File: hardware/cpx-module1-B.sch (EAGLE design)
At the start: 41 parts, among them IC2 MCP6004, IC3 LM4040DIM3-5.0, J1 WQP-PJ301M-12_JACK, J2 WQP-PJ301M-12_JACK, J3 WQP-PJ301M-12_JACK, J4 WQP-PJ301M-12_JACK, J5 WQP-PJ301M-12_JACK, J6 WQP-PJ301M-12_JACK, J7 WQP-PJ301M-12_JACK, J8 WQP-PJ301M-12_JACK, U1 CIRCUITPLAYGROUNDEXPRESS

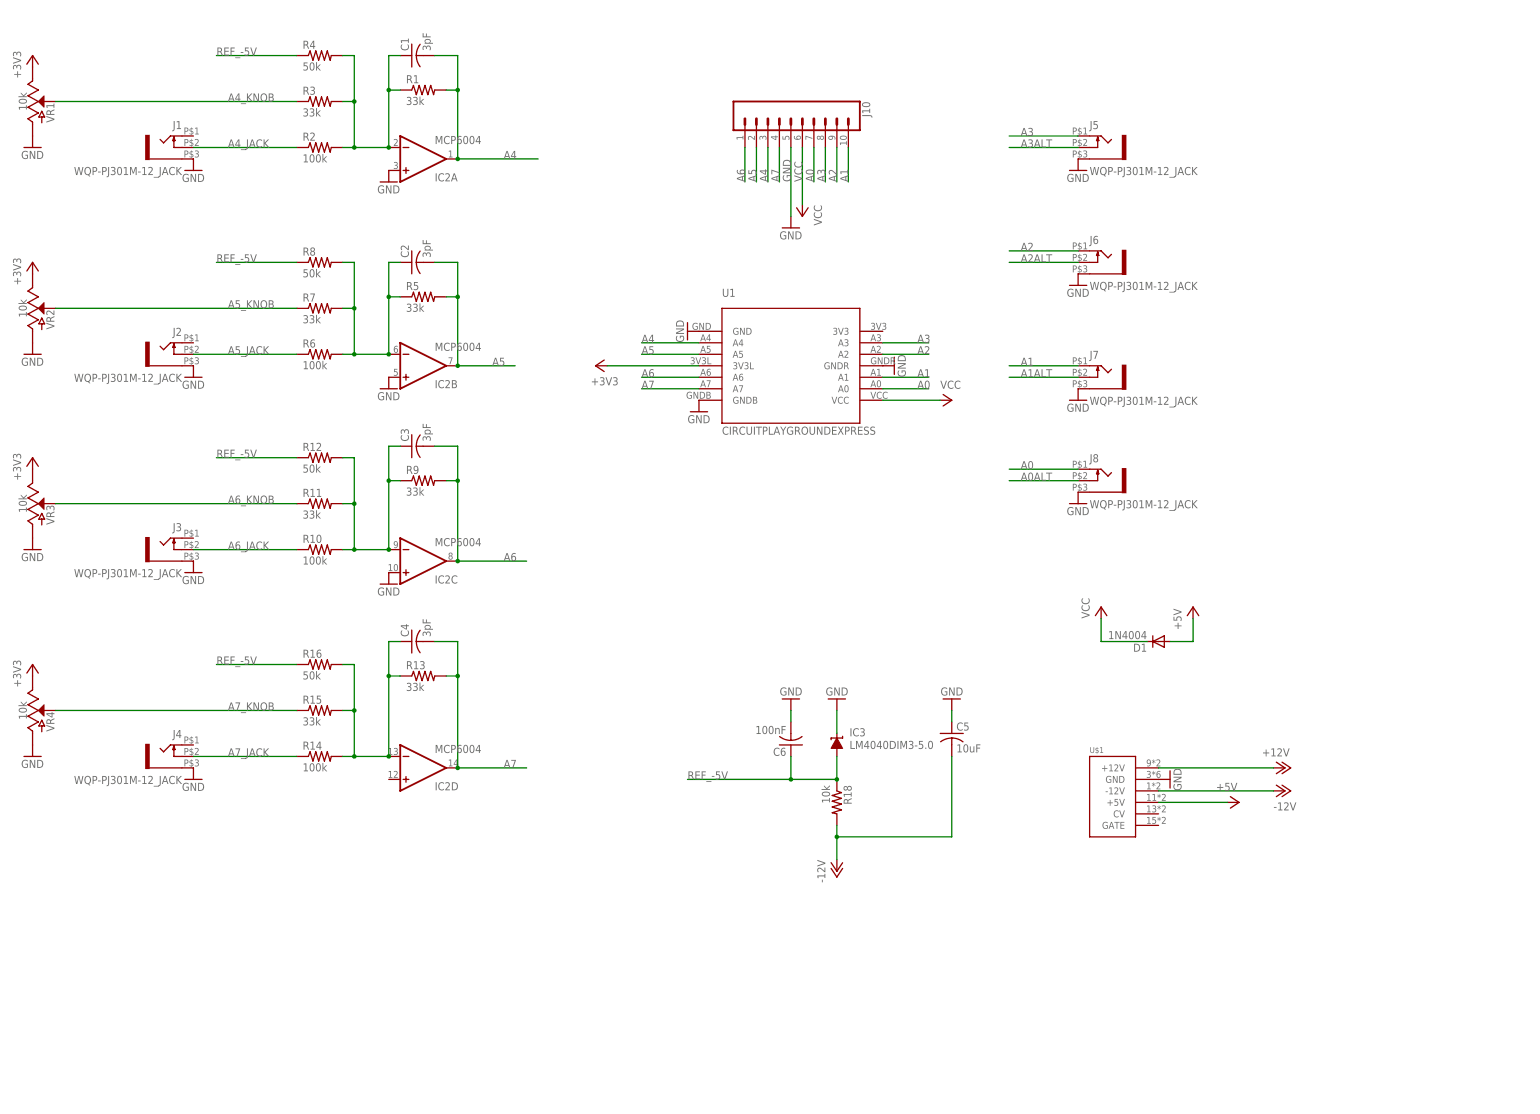
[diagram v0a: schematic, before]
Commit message: first cut at component placement
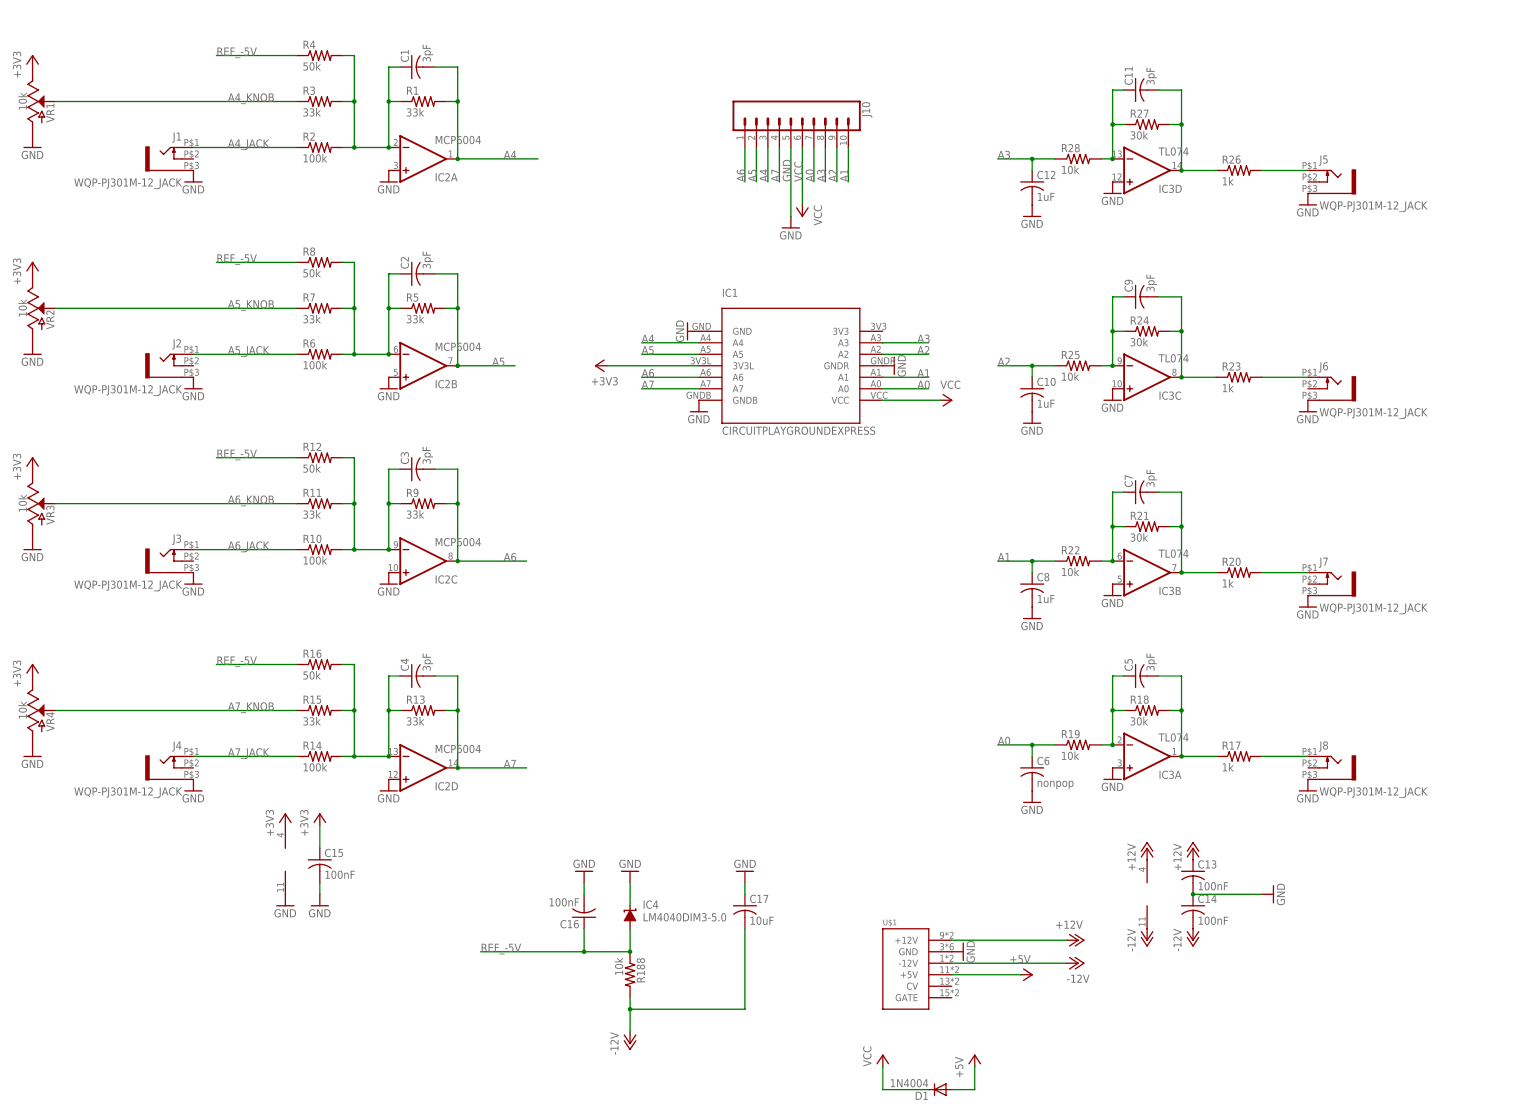
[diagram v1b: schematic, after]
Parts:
- added C10, C12, C8: 1uF, rcl:C-USC0603
- added C11, C7, C9: 3pF, rcl:C-USC0603
- added C13, C14, C15, C16: 100nF, rcl:C-USC0603
- added C17: 10uF, rcl:C-USC0603
- added IC4: LM4040DIM3-5.0, texas:LM4041B12DBZ
- added R17, R20, R23, R26: 1k, adafruit:R-US_R0603
- added R188, R19, R22, R25, R28: 10k, adafruit:R-US_R0603
- added R21, R24, R27: 30k, adafruit:R-US_R0603
- C5: value 10uF -> 3pF
- C6: value 100nF -> nonpop
- IC3: value LM4040DIM3-5.0 -> TL074; device texas:LM4041B12DBZ -> gm-ics:TL074D
- R18: value 10k -> 30k
- renumbered U1 to IC1
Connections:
- removed net A0ALT: J8.3
- removed net A1ALT: J7.3
- removed net A2ALT: J6.3
- removed net A3ALT: J5.3
- new net N$1: C5.2, IC3A.OUT, R17.1, R18.2
- new net N$10: C9.2, IC3C.OUT, R23.1, R24.2
- new net N$11: J7.2, R20.2
- new net N$12: C9.1, IC3C.-IN, R24.1, R25.2
- new net N$13: J6.2, R23.2
- new net N$14: C11.2, IC3D.OUT, R26.1, R27.2
- new net N$15: C11.1, IC3D.-IN, R27.1, R28.2
- new net N$16: J5.2, R26.2
- new net N$6: J8.2, R17.2
- new net N$7: C5.1, IC3A.-IN, R18.1, R19.2
- new net N$8: C7.2, IC3B.OUT, R20.1, R21.2
- new net N$9: C7.1, IC3B.-IN, R21.1, R22.2
- net +12V: now also C13.1, IC3P.V+
- net +3V3: now also C15.1, IC2P.V+
- net -12V: now also C14.2, C17.2, IC3P.V-, R188.2; no longer C5.2, R18.2
- net A0: now also C6.1, R19.1; no longer J8.2
- net A1: now also C8.1, R22.1; no longer J7.2
- net A2: now also C10.1, R25.1; no longer J6.2
- net A3: now also C12.1, R28.1; no longer J5.2
- net A4_JACK: now also J1.2; no longer J1.3
- net A5_JACK: now also J2.2; no longer J2.3
- net A6_JACK: now also J3.2; no longer J3.3
- net A7_JACK: now also J4.2; no longer J4.3
- net GND: now also C10.2, C12.2, C13.2, C14.1, C15.2, C16.2, C17.1, C8.2, IC2D.+IN, IC2P.V-, IC3A.+IN, IC3B.+IN, IC3C.+IN, IC3D.+IN, IC4.C; no longer C5.1, IC3.C
- net REF_-5V: now also C16.1, IC4.A, R188.1; no longer C6.1, IC3.A, R18.1
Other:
- moved on the sheet: C1, C2, C3, C4, C5, C6, D1, J1, J2, J3, J4, J5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

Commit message: autorouted as a test
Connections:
- net A4_KNOB: now also R3.1
- net A5_KNOB: now also R7.1
- net A6_KNOB: now also R11.1
- net A7_KNOB: now also R15.1
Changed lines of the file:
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@@
 <pinref part="VR1" gate="G$1" pin="S"/>
 <label x="-48.26" y="129.54" size="1.778" layer="95"/>
+<pinref part="R3" gate="G$1" pin="1"/>
 </segment>
 </net>
@@
 <pinref part="VR2" gate="G$1" pin="S"/>
 <label x="-48.26" y="83.82" size="1.778" layer="95"/>
+<pinref part="R7" gate="G$1" pin="1"/>
 </segment>
 </net>
@@
 <pinref part="VR3" gate="G$1" pin="S"/>
 <label x="-48.26" y="40.64" size="1.778" layer="95"/>
+<pinref part="R11" gate="G$1" pin="1"/>
 </segment>
 </net>
@@
 <pinref part="VR4" gate="G$1" pin="S"/>
 <label x="-48.26" y="-5.08" size="1.778" layer="95"/>
+<pinref part="R15" gate="G$1" pin="1"/>
 </segment>
 </net>

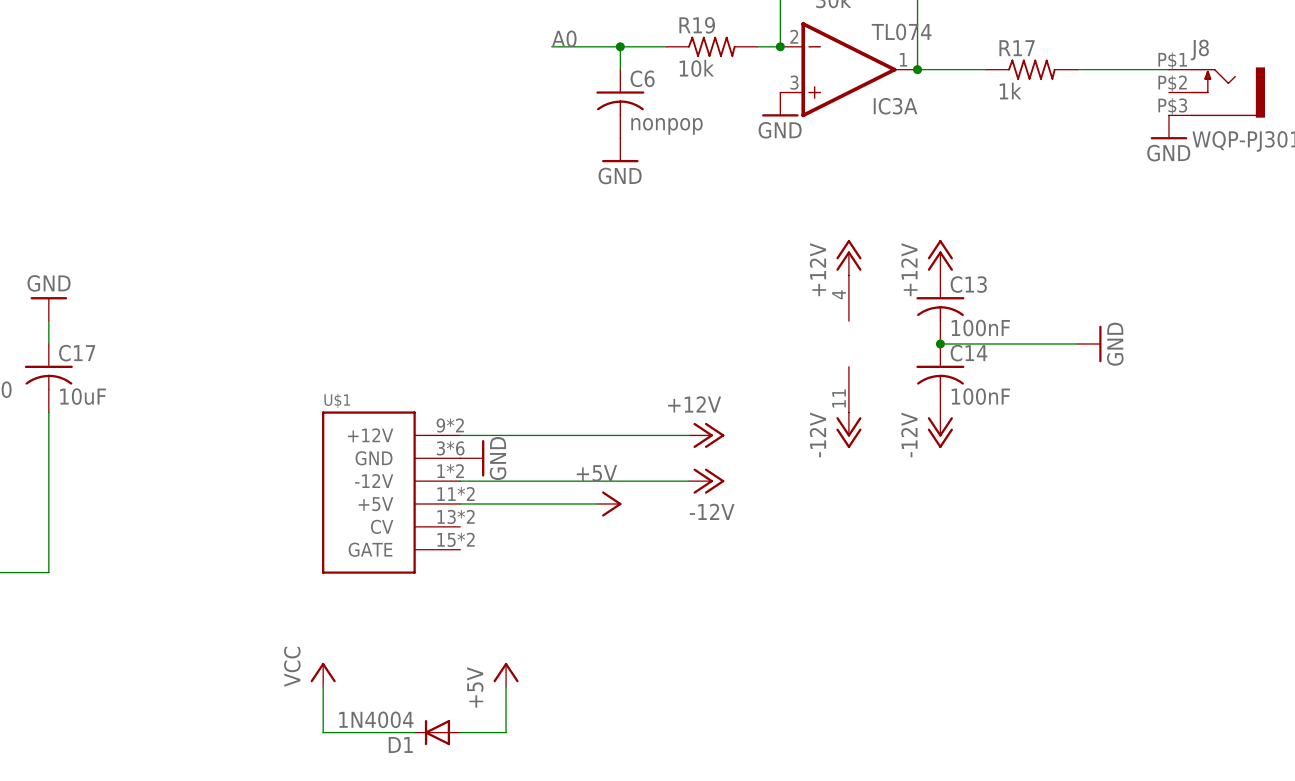
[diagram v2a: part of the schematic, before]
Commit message: added protection diodes and filter caps, added pdfs
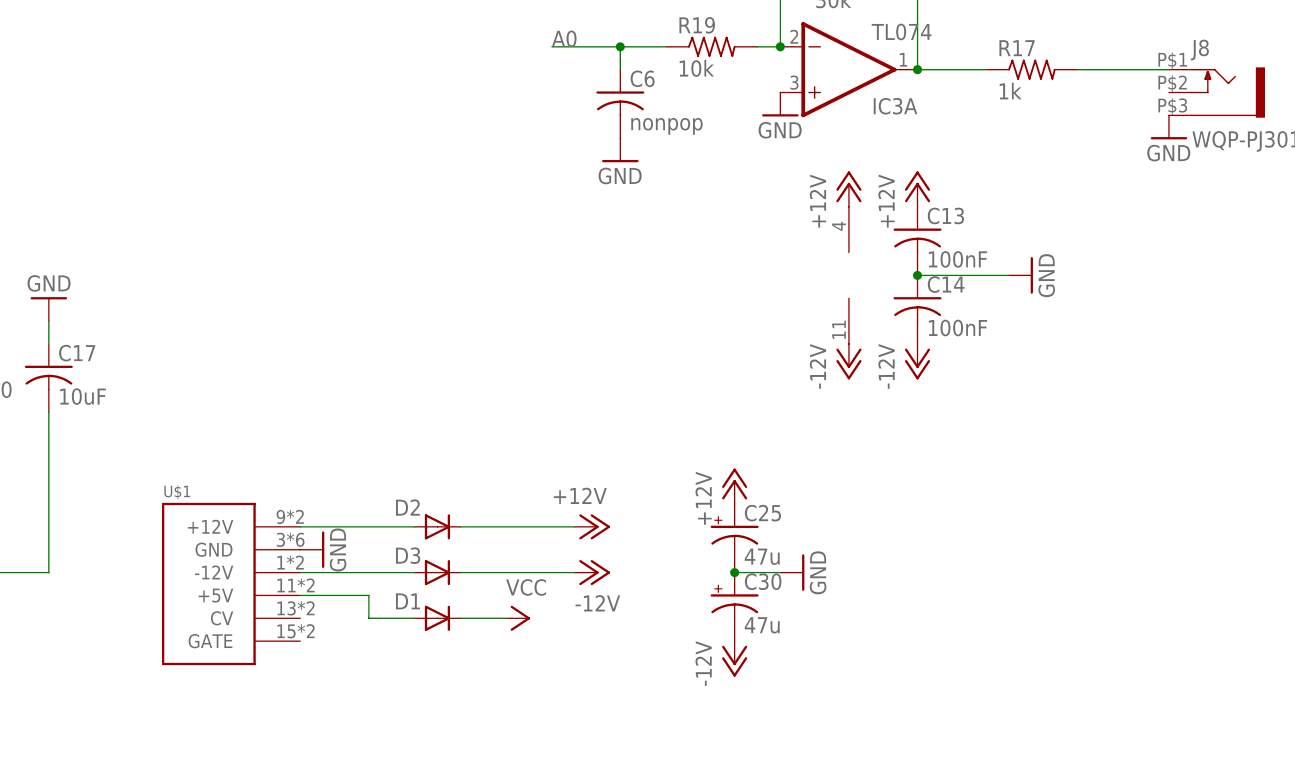
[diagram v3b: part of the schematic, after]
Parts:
- added C25, C30: 47u, rcl:CPOL-USD
- added D2, D3: 1N5819HW, diode:DIODE-SOD123
- D1: value 1N4004 -> 1N5819HW; device adafruit:1N4004 -> diode:DIODE-SOD123
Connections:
- net +5V renamed N$19
- new net N$17: D2.A, U$1.+12V
- new net N$18: D3.A, U$1.-12V
- net +12V: now also C25.+, D2.C; no longer U$1.+12V
- net -12V: now also C30.-, D3.C; no longer U$1.-12V
- net GND: now also C25.-, C30.+
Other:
- moved on the sheet: C13, C14, U$1

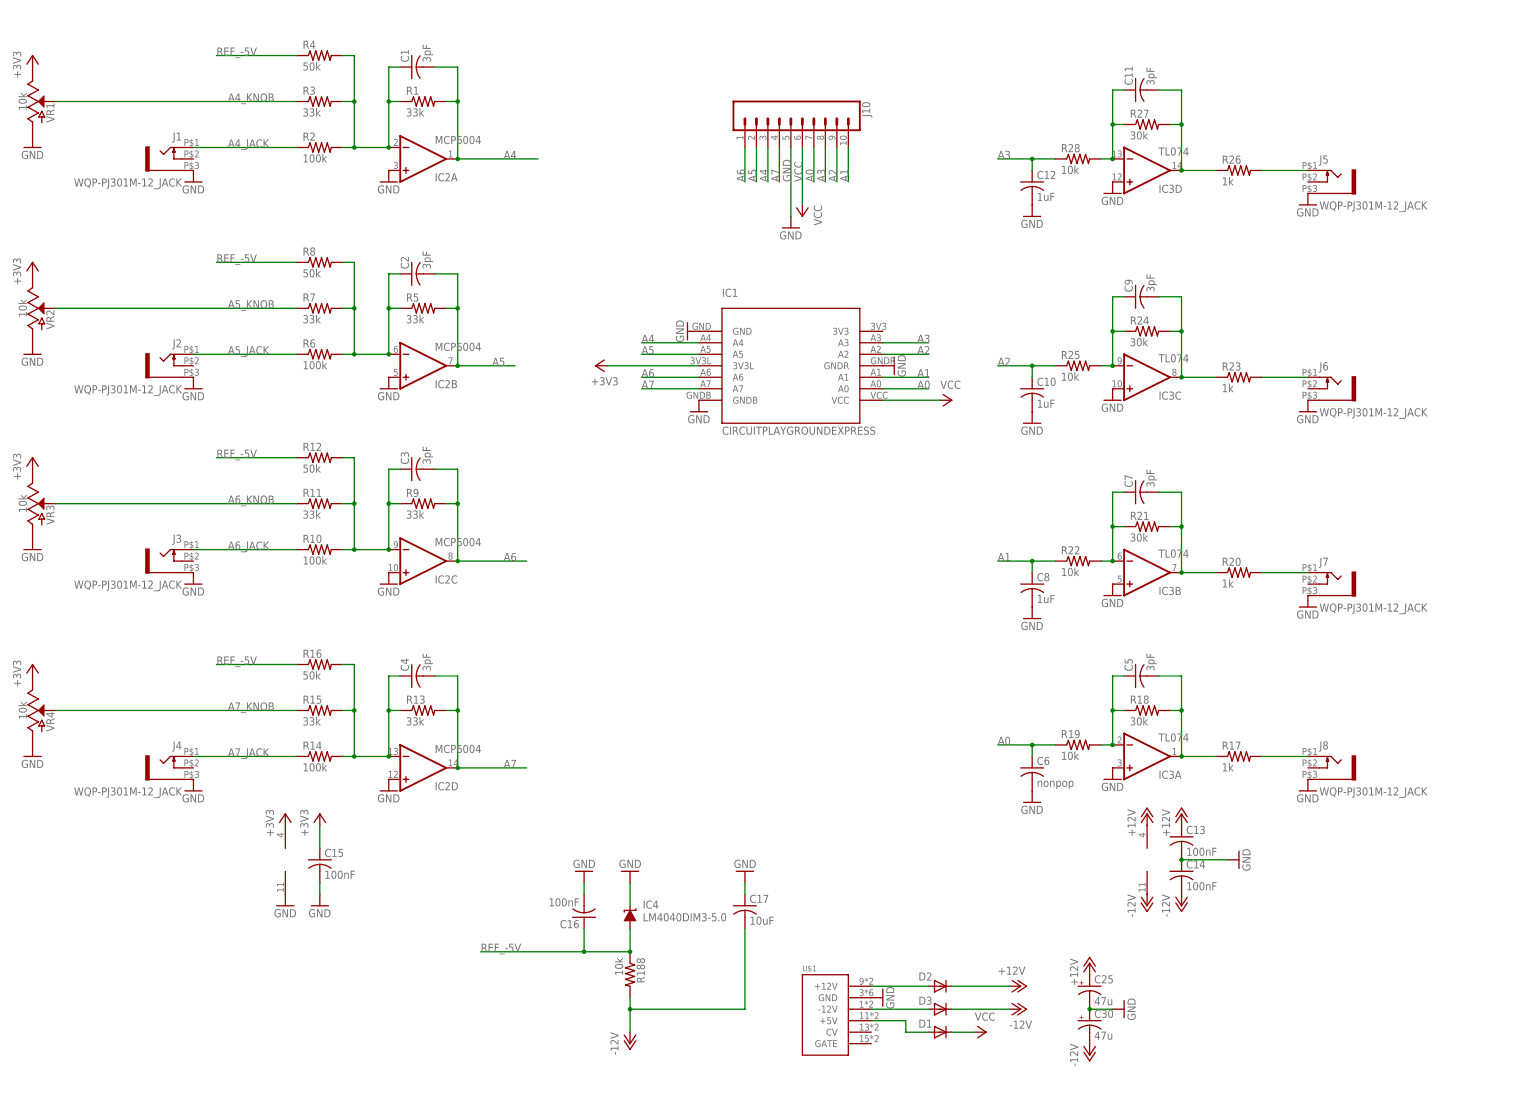
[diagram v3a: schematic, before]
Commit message: added resistors on A1,A2,A3 to potentially allow touch input to work, re-routed lower half a bit better
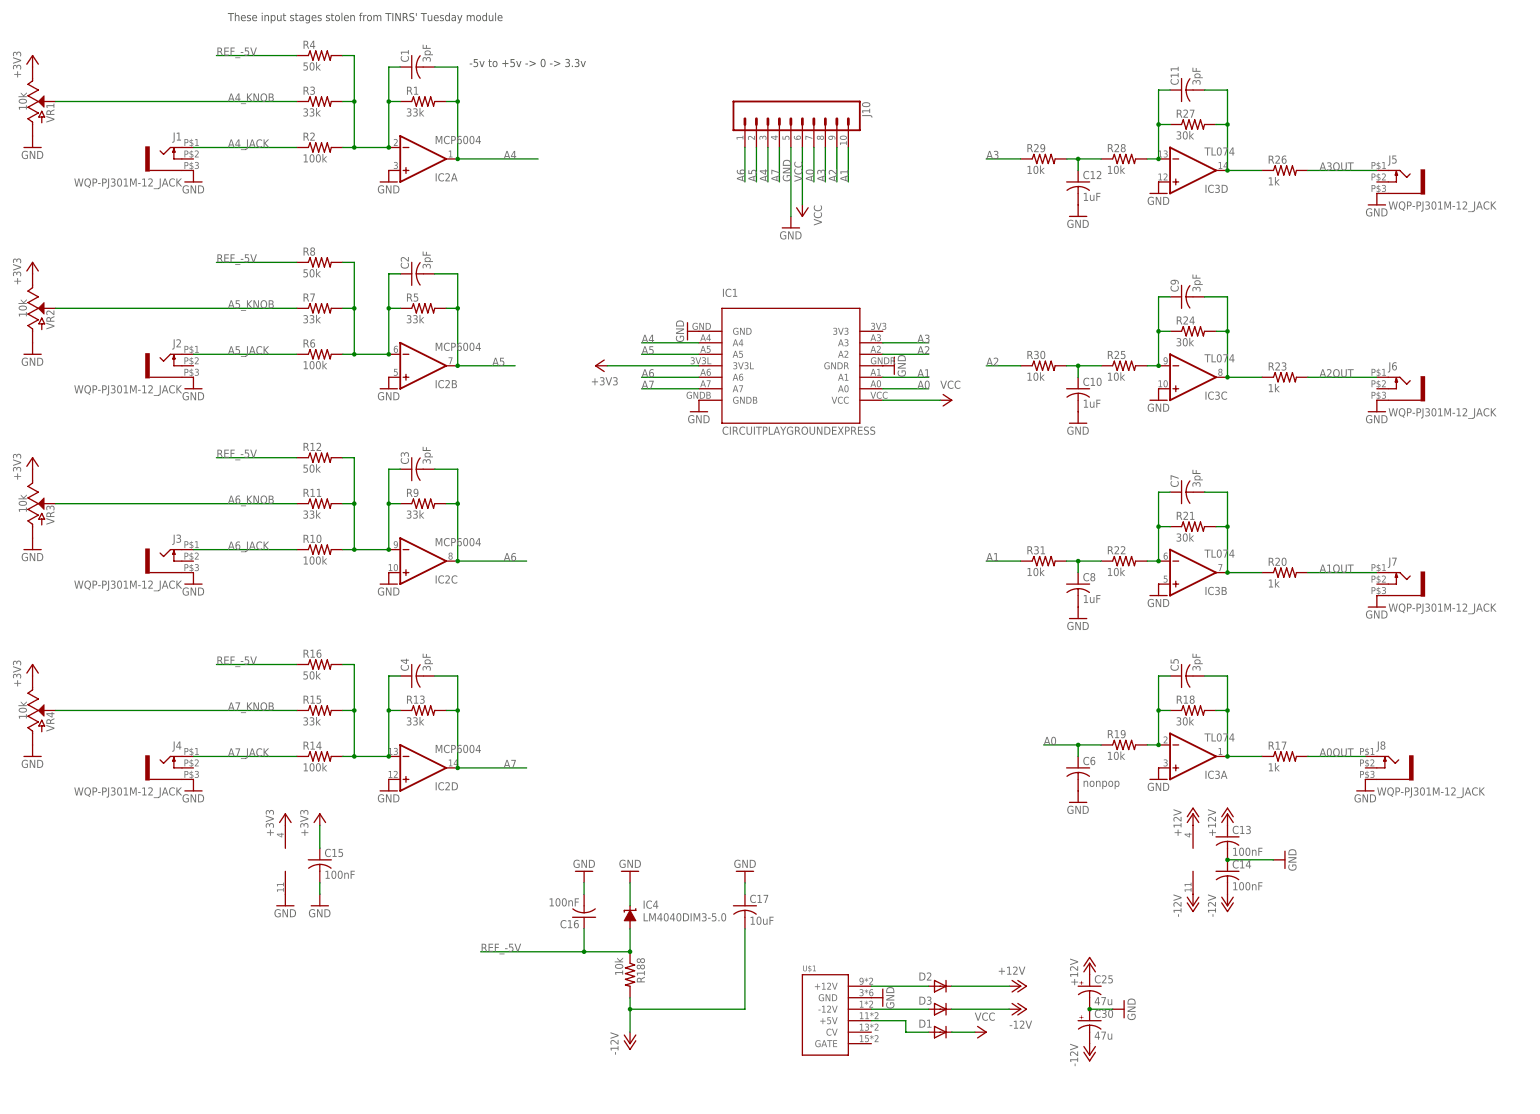
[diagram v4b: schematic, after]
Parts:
- added R29, R30, R31: 10k, adafruit:R-US_R0603
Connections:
- net N$11 renamed A1OUT
- net N$13 renamed A2OUT
- net N$16 renamed A3OUT
- net N$6 renamed A0OUT
- new net N$20: C12.1, R28.1, R29.2
- new net N$21: C10.1, R25.1, R30.2
- new net N$22: C8.1, R22.1, R31.2
- net A1: now also R31.1; no longer C8.1, R22.1
- net A2: now also R30.1; no longer C10.1, R25.1
- net A3: now also R29.1; no longer C12.1, R28.1
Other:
- note added: "-5v to +5v -> 0 -> 3.3v"
- note added: "These input stages stolen from TINRS' Tuesday module"
- moved on the sheet: C10, C11, C12, C13, C14, C5, C6, C7, C8, C9, IC3A, IC3B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
